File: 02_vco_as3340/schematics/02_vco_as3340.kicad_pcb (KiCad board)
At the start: 2 copper layers, 75 x 100 mm, 80 parts, among them J5 inputs, J6 Panel Power, J7 Outputs, Q1 BC547C, Q2 BC547C, U1 TL072, U2 AS3340, U3 TL074

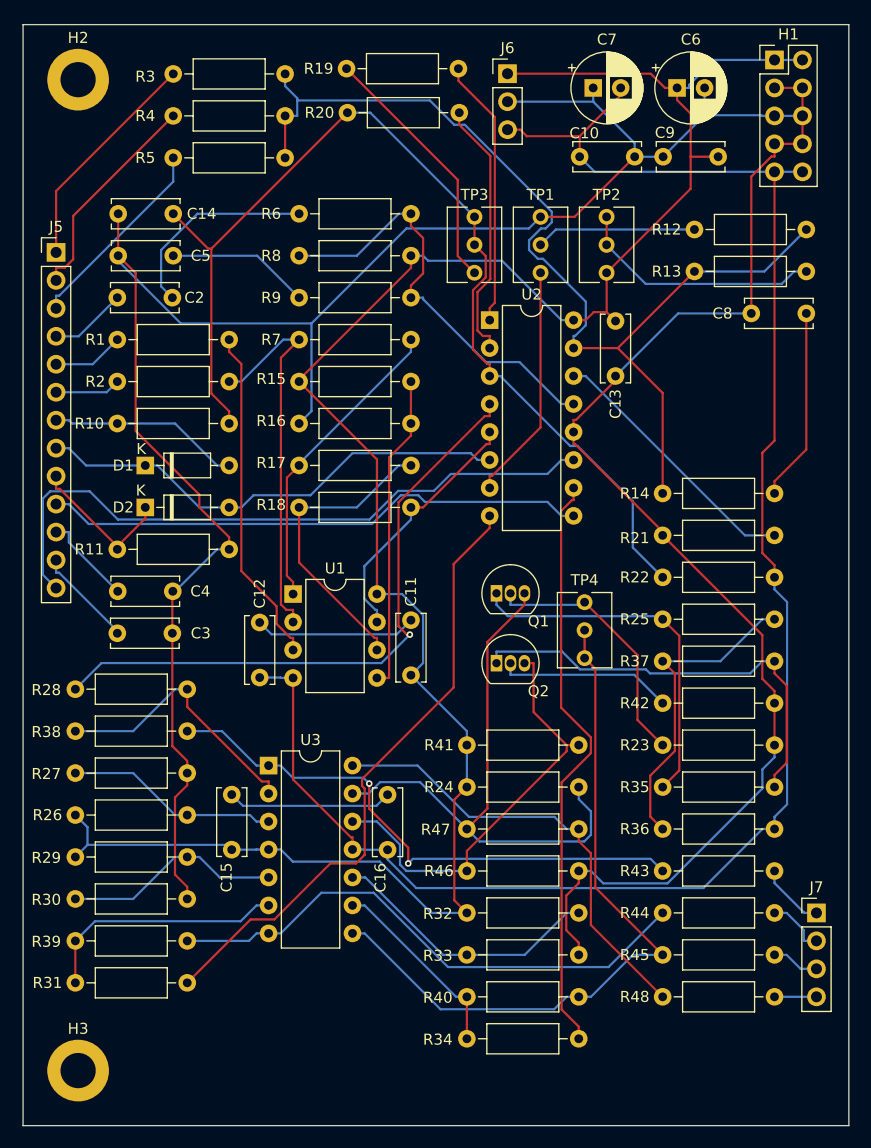
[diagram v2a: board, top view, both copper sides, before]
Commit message: updated PCBs for 02 and 03
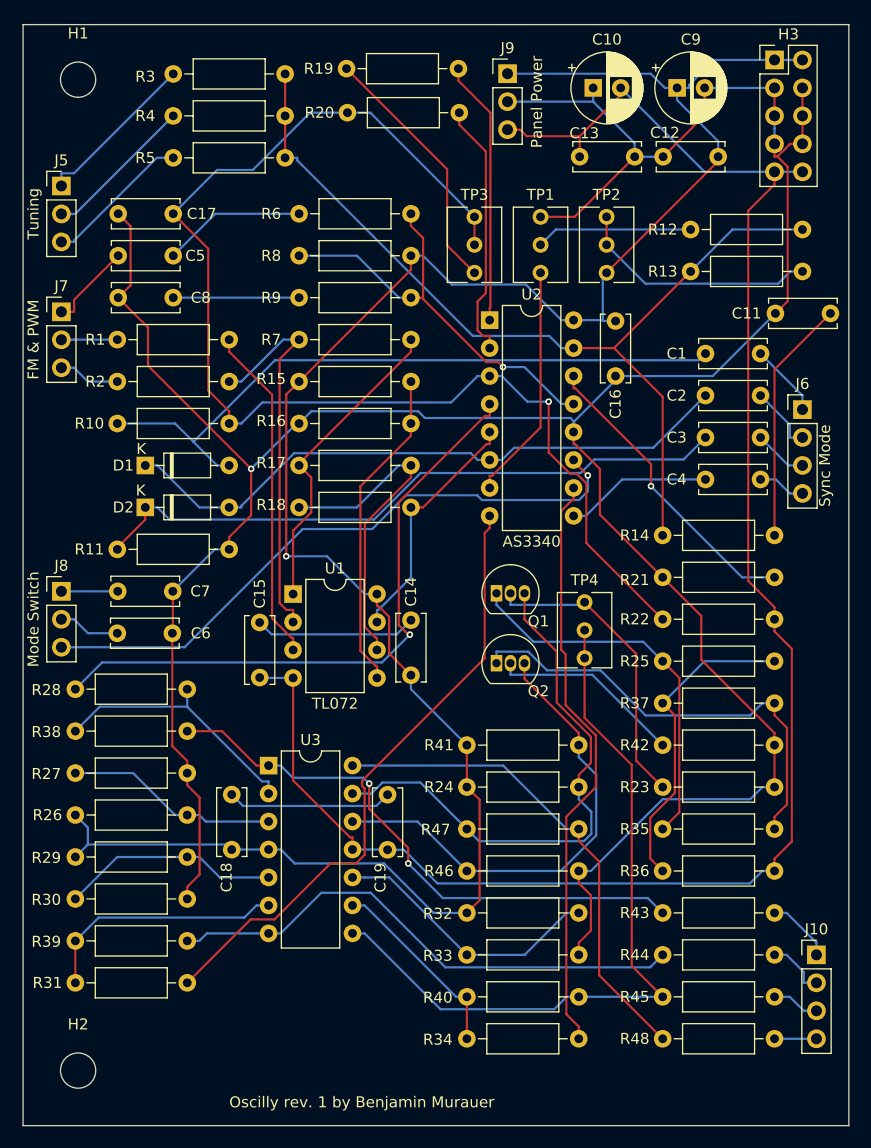
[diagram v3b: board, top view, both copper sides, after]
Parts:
- added C1: 1nF, Capacitor_THT:C_Disc_D6.0mm_W2.5mm_P5.00mm, F.Cu at (89.0, 55.9)
- added C2: 1nF, Capacitor_THT:C_Disc_D6.0mm_W2.5mm_P5.00mm, F.Cu at (89.0, 59.7)
- added C3: 1nF, Capacitor_THT:C_Disc_D6.0mm_W2.5mm_P5.00mm, F.Cu at (89.0, 63.5)
- added C4: 1nF, Capacitor_THT:C_Disc_D6.0mm_W2.5mm_P5.00mm, F.Cu at (89.0, 67.3)
- added J6: Sync Mode, Connector_PinHeader_2.54mm:PinHeader_1x04_P2.54mm_Vertical, F.Cu at (97.8, 61.0)
- added J7: FM & PWM, Connector_PinHeader_2.54mm:PinHeader_1x03_P2.54mm_Vertical, F.Cu at (30.5, 52.1)
- added J8: Mode Switch, Connector_PinHeader_2.54mm:PinHeader_1x03_P2.54mm_Vertical, F.Cu at (30.5, 77.5)
- H1: renamed from H2; footprint MountingHole:MountingHole_3.2mm_M3_DIN965_Pad -> MountingHole:MountingHole_3.2mm_M3
- H2: renamed from H3; footprint MountingHole:MountingHole_3.2mm_M3_DIN965_Pad -> MountingHole:MountingHole_3.2mm_M3
- J5: value inputs -> Tuning; footprint Connector_PinHeader_2.54mm:PinHeader_1x13_P2.54mm_Vertical -> Connector_PinHeader_2.54mm:PinHeader_1x03_P2.54mm_Vertical
- moved J5 6.05 mm to (30.5, 40.7)
- moved C5 3.81 mm to (40.6, 47.0)
- moved R14 3.81 mm to (85.1, 72.4)
- moved R21 3.81 mm to (85.1, 76.2)
- moved R22 3.81 mm to (85.1, 80.0)
- moved R23 3.81 mm to (85.1, 95.2)
- moved R35 3.81 mm to (85.1, 99.1)
- moved R36 3.81 mm to (85.1, 102.9)
- moved R37 3.81 mm to (85.1, 87.6)
- moved R42 3.81 mm to (85.1, 91.4)
- moved R43 3.81 mm to (85.1, 106.7)
- moved R45 3.81 mm to (85.1, 114.3)
- moved R48 3.81 mm to (85.1, 118.1)
- moved C8 3.81 mm to (35.6, 50.8)
- moved J10 3.81 mm to (99.1, 110.5)
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- renumbered C7 to C10, C8 to C11, C9 to C12, C10 to C13, C11 to C14, C12 to C15, C13 to C16, C14 to C17, C15 to C18, C16 to C19, C2 to C5, C3 to C6, C4 to C7, C5 to C8, C6 to C9, H1 to H3, J7 to J10, J6 to J9
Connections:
- D1 pad 1: /PCB/Hard Sync -> Net-(D1-K)
- D1 pad 2: /PCB/Positive Hard Sync -> Net-(D1-A)
- D2 pad 1: /PCB/Negative Hard Sync -> Net-(D2-K)
- D2 pad 2: /PCB/Hard Sync -> Net-(D1-K)
- R10 pad 1: /PCB/Positive Hard Sync -> Net-(D1-A)
- R11 pad 1: /PCB/Negative Hard Sync -> Net-(D2-K)
- U2 pad 6: /PCB/Hard Sync -> Net-(D1-K)
- U2 pad 9: /PCB/Soft Sync -> Net-(U2-VSSI)
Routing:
- net Net-(D1-A): track 0.00 -> 61.6 mm
- net Net-(D2-K): track 0.00 -> 59.3 mm
- net Net-(D1-K): track 0.00 -> 57.3 mm
- net /PCB/Soft Sync: track 49.6 -> 4.34 mm
- net /PCB/Hard Sync: track 43.9 -> 6.06 mm
- net Net-(U2-VEE): track 96.2 -> 115.0 mm, vias 0 -> 1
- net GND: track 289.1 -> 270.7 mm, vias 0 -> 1
- net Net-(U2-VSSI): track 0.00 -> 13.4 mm
- net /PCB/Positive Hard Sync: track 17.4 -> 6.66 mm
- net /PCB/Negative Hard Sync: track 13.8 -> 4.86 mm
- net Net-(U2-VFCI): track 93.4 -> 85.2 mm
- net /PCB/Coarse Tune: track 19.8 -> 13.8 mm
- net Net-(C5-Pad1): track 18.6 -> 13.0 mm
- net /PCB/1V/O: track 20.6 -> 15.0 mm
- net /PCB/Fine Tune: track 18.2 -> 13.4 mm
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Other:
- board text added: "Oscilly rev. 1 by Benjamin Murauer"

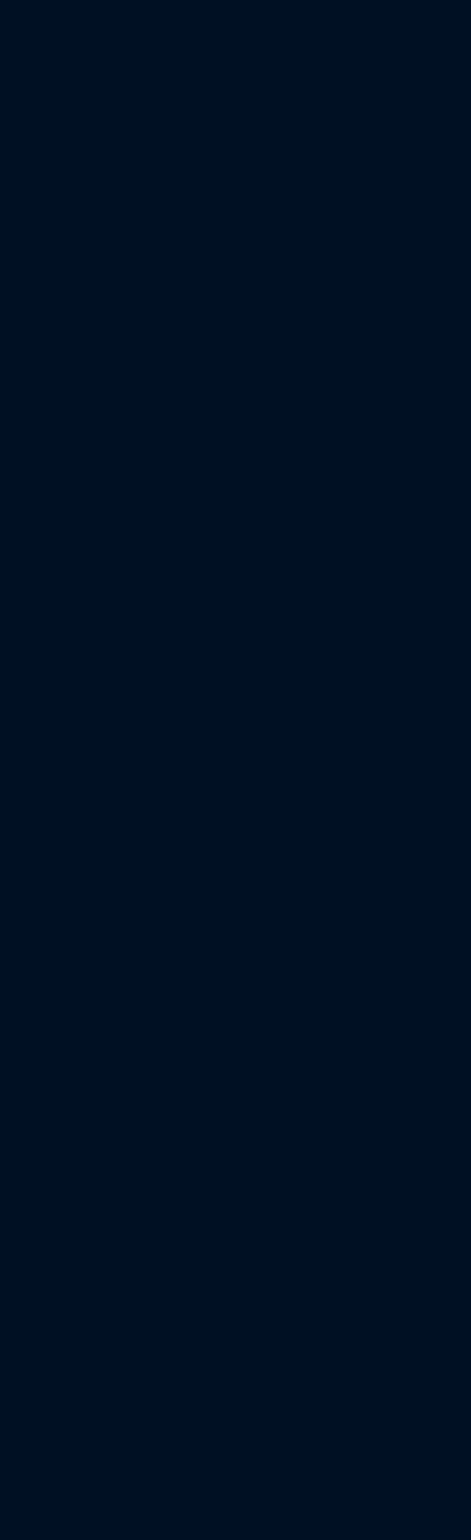
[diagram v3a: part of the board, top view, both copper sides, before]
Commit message: split 02 into subboard
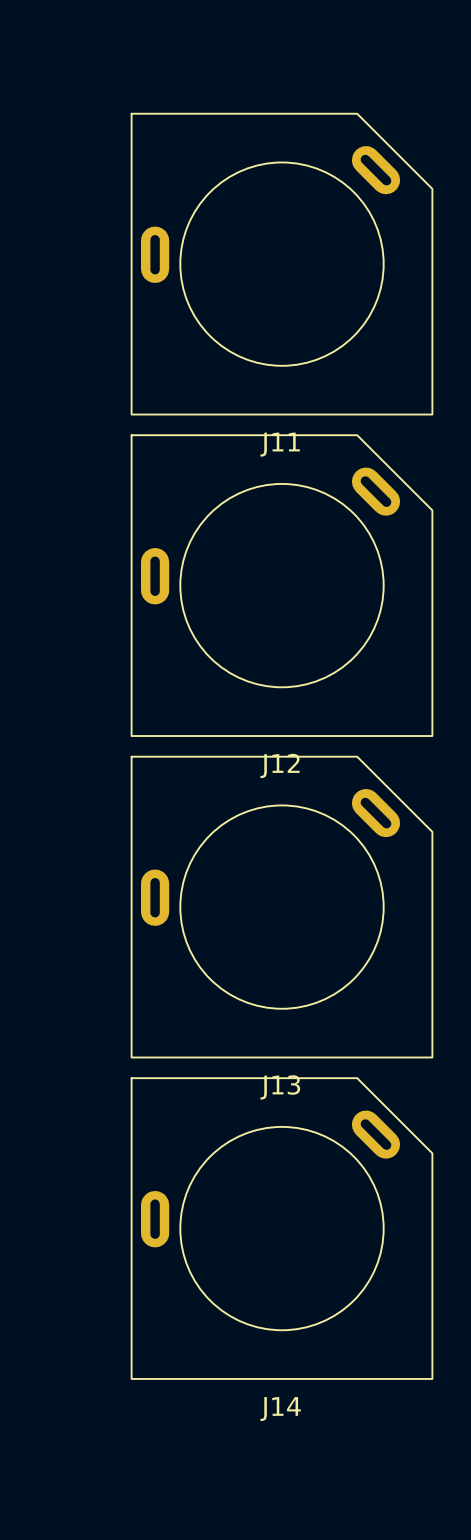
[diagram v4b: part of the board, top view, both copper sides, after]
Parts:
- added J11: SQUARE OUT, cynthia:6.35 mm jack socket mono, F.Cu at (134.7, 40.1)
- added J12: TRI OUT, cynthia:6.35 mm jack socket mono, F.Cu at (134.7, 57.2)
- added J13: SAW OUT, cynthia:6.35 mm jack socket mono, F.Cu at (134.7, 74.3)
- added J14: SINE OUT, cynthia:6.35 mm jack socket mono, F.Cu at (134.7, 91.4)
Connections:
- R43 pad 2: /PCB/Square -> /Output Board/SQUARE
- R44 pad 2: /PCB/Saw -> /Output Board/SAW
- R45 pad 2: /PCB/Triangle -> /Output Board/TRI
- R48 pad 2: /PCB/Sine -> /Output Board/SINE
